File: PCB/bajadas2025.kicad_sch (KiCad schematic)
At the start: 11 parts, among them J1 Toggle Switch, J2 Data/Power Connection

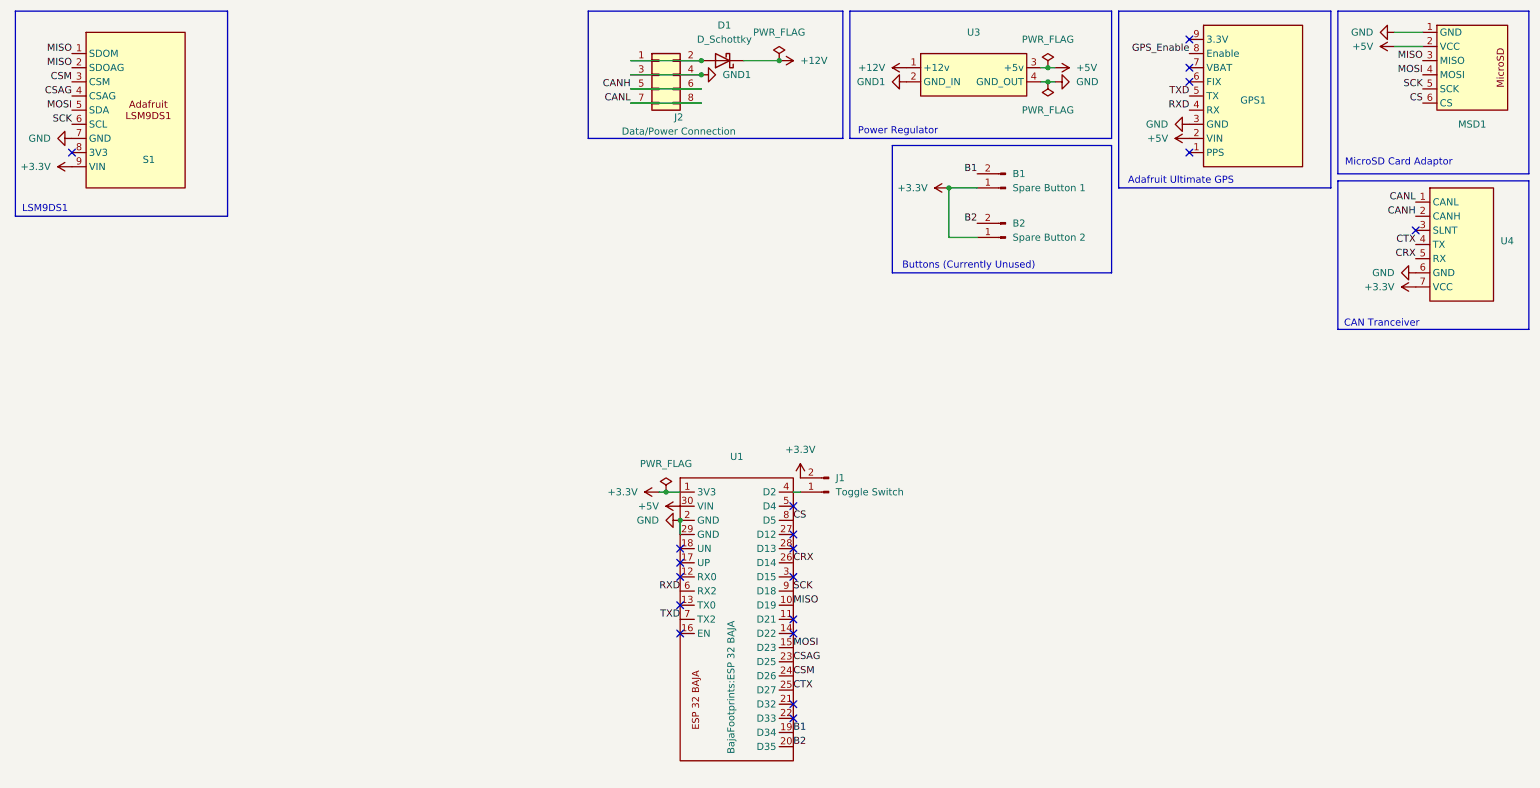
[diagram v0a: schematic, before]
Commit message: Various Modifications
Update Data/Power Connection to use pads

Update spare buttons to use pads

Update spare buttons to be tied to ground (to use internal pullup)

Fix Ultimate GPS to use GPS_RX->ESP32_TX and GPS_TX-ESP32_RX

Connect GPS_FIX to an arbitrary GPIO input pin in case we want to use it in the future

Add pads for toggle switch

Add second set of pads for auxiliary aviation plug connector

Update positioning of components on PCB

Add voltage divider circuit for measuring battery voltage

Move CAN-TX and CAN-RX to standardized GPIO
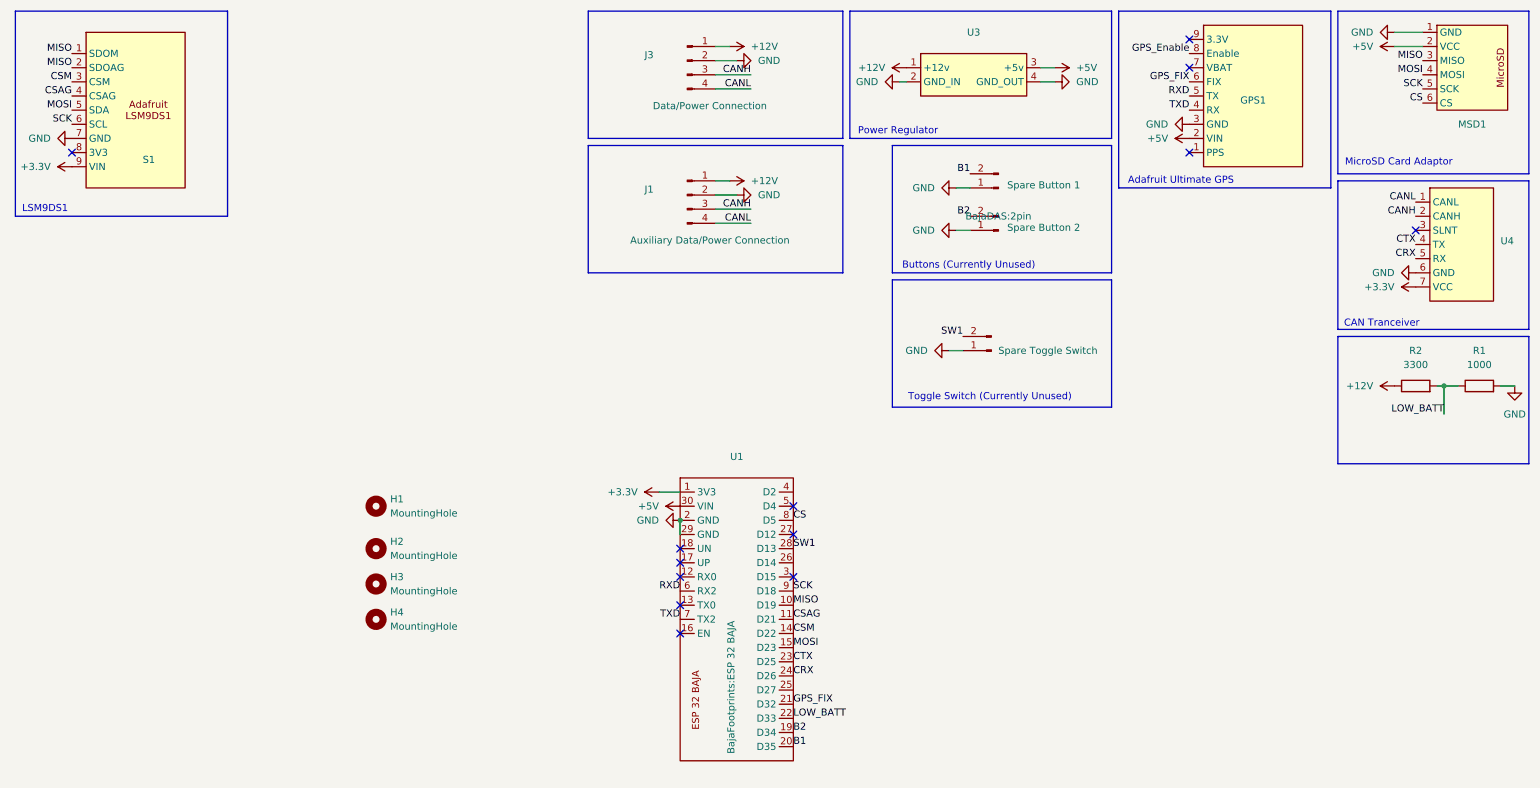
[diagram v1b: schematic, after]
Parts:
- removed B1: Spare Button 1, Connector_PinHeader_2.54mm:PinHeader_1x02_P2.54mm_Vertical, symbol Connector:Conn_01x02_Pin
- removed B2: Spare Button 2, Connector_PinHeader_2.54mm:PinHeader_1x02_P2.54mm_Vertical, symbol Connector:Conn_01x02_Pin
- removed D1: D_Schottky, Diode_THT:D_DO-201_P12.70mm_Horizontal, symbol Device:D_Schottky
- removed J1: Toggle Switch, symbol Connector:Conn_01x02_Pin
- removed J2: Data/Power Connection, Connector_PinHeader_2.54mm:PinHeader_2x04_P2.54mm_Vertical, symbol Connector_Generic:Conn_02x04_Odd_Even
- added H1, H2, H3, H4: MountingHole, MountingHole:MountingHole_4.3mm_M4, symbol Mechanical:MountingHole
- added J1: Auxiliary Data/Power Connection, BajaDAS:4pin, symbol Connector:Conn_01x04_Pin
- added J2: Spare Button 1, BajaDAS:2pin, symbol Connector:Conn_01x03_Pin
- added J3: Data/Power Connection, BajaDAS:4pin, symbol Connector:Conn_01x04_Pin
- added J4: Spare Button 2, BajaDAS:2pin, symbol Connector:Conn_01x03_Pin
- added J5: Spare Toggle Switch, BajaDAS:2pin, symbol Connector:Conn_01x03_Pin
- added R1: 1000, Resistor_THT:R_Axial_DIN0207_L6.3mm_D2.5mm_P10.16mm_Horizontal, symbol Device:R
- added R2: 3300, Resistor_THT:R_Axial_DIN0207_L6.3mm_D2.5mm_P10.16mm_Horizontal, symbol Device:R
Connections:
- net GND1 is gone; now on net GND: U3.2 (GND_IN)
- net +12V: now also J1.1 (Pin_1), J3.1 (Pin_1), R2.1
- net B1: now also U1.20 (D35), J2.2 (Pin_2); no longer U1.19 (D34)
- net B2: now also U1.19 (D34), J4.2 (Pin_2); no longer U1.20 (D35)
- net CANH: now also J1.3 (Pin_3), J3.3 (Pin_3)
- net CANL: now also J1.4 (Pin_4), J3.4 (Pin_4)
- net CRX: now also U1.24 (D26); no longer U1.26 (D14)
- net CSAG: now also U1.11 (D21); no longer U1.23 (D25)
- net CSM: now also U1.14 (D22); no longer U1.24 (D26)
- net CTX: now also U1.23 (D25); no longer U1.25 (D27)
- net GND: now also J1.2 (Pin_2), J2.1 (Pin_1), J3.2 (Pin_2), J4.1 (Pin_1), J5.1 (Pin_1), R1.2
- net RXD: now also GPS1.5 (TX); no longer GPS1.4 (RX)
- net TXD: now also GPS1.4 (RX); no longer GPS1.5 (TX)
- net GPS_FIX: now reaches U1.21 (D32)
- net GPS_FIX: now also GPS1.6 (FIX)
- net LOW_BATT: now reaches U1.22 (D33)
- net LOW_BATT: now also R1.1, R2.2
- net SW1: now reaches U1.28 (D13)
- net SW1: now also J5.2 (Pin_2)
- no-connect marks 19 -> 13
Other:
- note added: "Toggle Switch (Currently Unused)"
